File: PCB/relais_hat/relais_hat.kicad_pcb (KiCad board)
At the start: 2 copper layers, 85 x 56 mm, 57 parts, among them J1 Conn_01x03, J10 Conn_01x02, J11 Conn_01x02, J12 Conn_01x03, J13 DB9_Female, J14 Conn_01x02, J2 Conn_01x03, J3 Conn_02x04_Odd_Even, J4 Screw_Terminal_01x02, J5 Screw_Terminal_01x02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

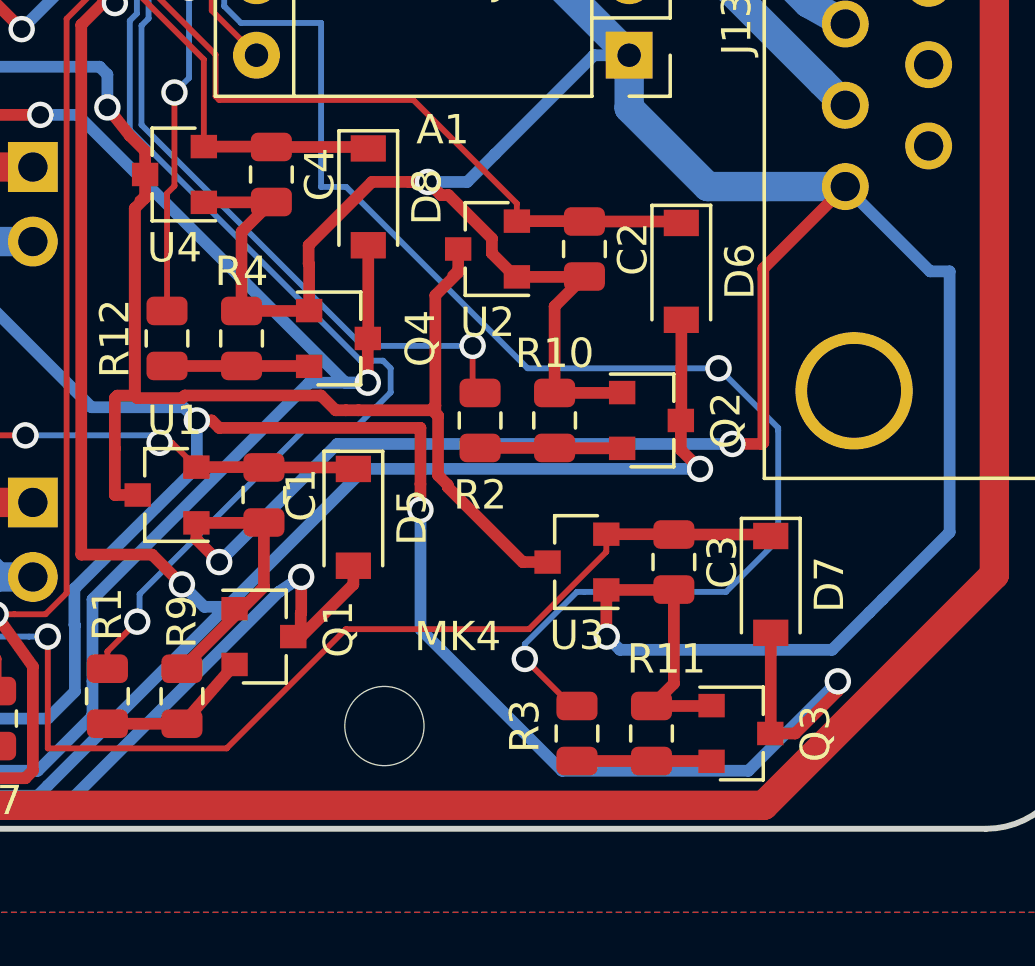
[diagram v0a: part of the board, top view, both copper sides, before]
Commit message: Q1/2/3/4 orientation correction
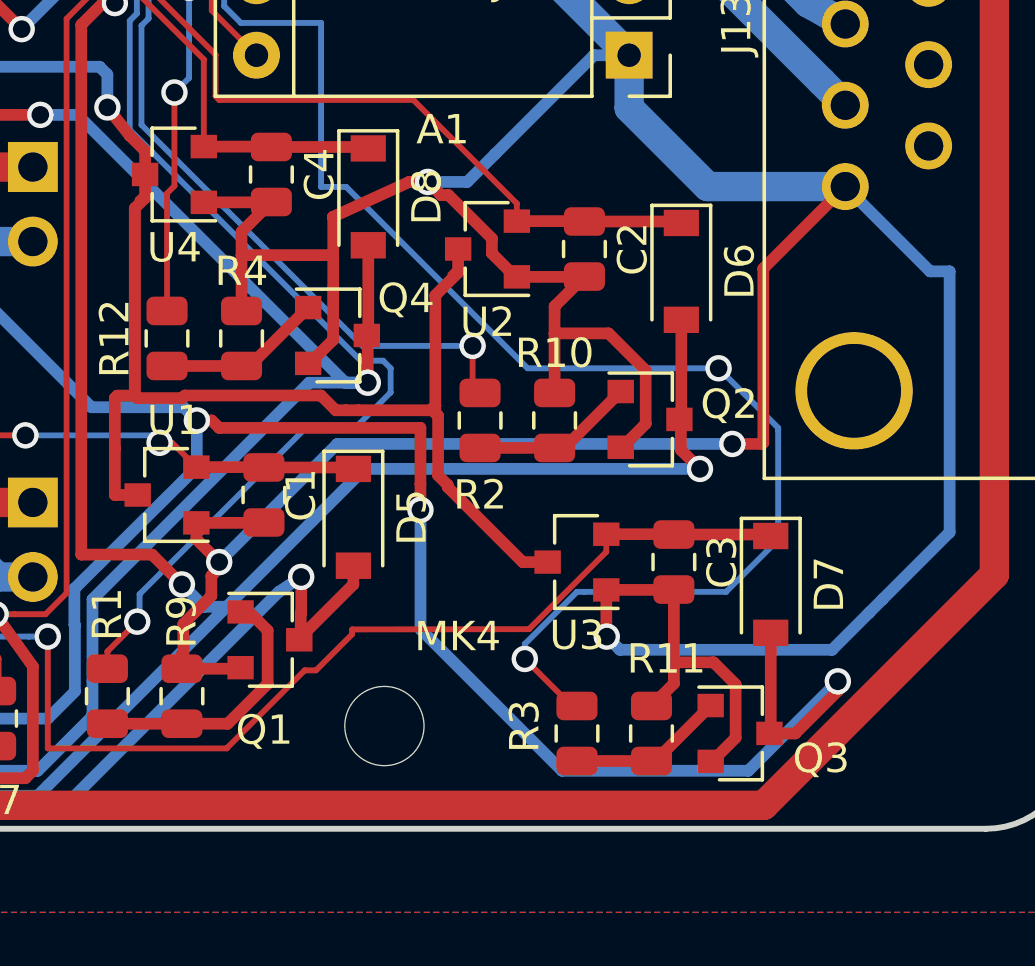
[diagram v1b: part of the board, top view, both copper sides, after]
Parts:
- moved Q1 0.23 mm to (257.6, 143.3)
- moved Q4 0.11 mm to (259.9, 132.9)
- moved Q2 0.06 mm to (270.6, 135.7)
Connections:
- A1 pad 2: Net-(A1-Pad2) -> (no net)
- A1 pad 9: Net-(A1-Pad9) -> (no net)
- J13 pad 6: Net-(J13-Pad6) -> (no net)
- J13 pad 7: Net-(J13-Pad7) -> (no net)
- J13 pad 8: Net-(J13-Pad8) -> (no net)
- J13 pad 9: Net-(J13-Pad9) -> (no net)
- K1 pad 5: Net-(K1-Pad5) -> (no net)
- K2 pad 5: Net-(K2-Pad5) -> (no net)
- K3 pad 5: Net-(K3-Pad5) -> (no net)
- K4 pad 5: Net-(K4-Pad5) -> (no net)
- P1 pad 10: /UART_RX -> (no net)
- P1 pad 19: /UART_TX_NanopiM4 -> (no net)
- P1 pad 21: /UART_RX_NanopiM4 -> (no net)
- P1 pad 23: Net-(P1-Pad23) -> (no net)
- P1 pad 24: Net-(P1-Pad24) -> (no net)
- P1 pad 26: Net-(P1-Pad26) -> (no net)
- P1 pad 27: Net-(P1-Pad27) -> (no net)
- P1 pad 28: Net-(P1-Pad28) -> (no net)
- P1 pad 29: Net-(P1-Pad29) -> (no net)
- P1 pad 3: /SDA -> (no net)
- P1 pad 31: Net-(P1-Pad31) -> (no net)
- P1 pad 32: Net-(P1-Pad32) -> (no net)
- P1 pad 33: Net-(P1-Pad33) -> (no net)
- P1 pad 35: Net-(P1-Pad35) -> (no net)
- P1 pad 36: Net-(P1-Pad36) -> (no net)
- P1 pad 37: Net-(P1-Pad37) -> (no net)
- P1 pad 38: Net-(P1-Pad38) -> (no net)
- P1 pad 40: Net-(P1-Pad40) -> (no net)
- P1 pad 5: /SCL -> (no net)
- P1 pad 7: /1-wire -> (no net)
- P1 pad 8: /UART_TX -> (no net)
- Q1 pad 1: GND -> Net-(Q1-Pad1)
- Q1 pad 2: Net-(Q1-Pad2) -> GND
- Q2 pad 1: GND -> Net-(Q2-Pad1)
- Q2 pad 2: Net-(Q2-Pad2) -> GND
- Q3 pad 1: GND -> Net-(Q3-Pad1)
- Q3 pad 2: Net-(Q3-Pad2) -> GND
- Q4 pad 1: GND -> Net-(Q4-Pad1)
- Q4 pad 2: Net-(Q4-Pad2) -> GND
- R1 pad 2: Net-(Q1-Pad2) -> Net-(Q1-Pad1)
- R10 pad 1: Net-(Q2-Pad2) -> Net-(Q2-Pad1)
- R11 pad 1: Net-(Q3-Pad2) -> Net-(Q3-Pad1)
- R12 pad 1: Net-(Q4-Pad2) -> Net-(Q4-Pad1)
- R2 pad 2: Net-(Q2-Pad2) -> Net-(Q2-Pad1)
- R3 pad 2: Net-(Q3-Pad2) -> Net-(Q3-Pad1)
- R4 pad 2: Net-(Q4-Pad2) -> Net-(Q4-Pad1)
- R9 pad 1: Net-(Q1-Pad2) -> Net-(Q1-Pad1)
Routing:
- net GND: track 269.2 -> 281.5 mm
- net Net-(Q1-Pad1): track 0.00 -> 9.05 mm
- net Net-(Q4-Pad1): track 0.00 -> 5.65 mm
- net Net-(Q2-Pad1): track 0.00 -> 5.63 mm
- net Net-(Q3-Pad1): track 0.00 -> 5.36 mm
- net Net-(Q1-Pad2): track 5.25 -> 0.00 mm
- net Net-(Q2-Pad2): track 4.85 -> 0.00 mm
- net Net-(Q4-Pad2): track 4.85 -> 0.00 mm
- net Net-(Q3-Pad2): track 4.59 -> 0.00 mm
